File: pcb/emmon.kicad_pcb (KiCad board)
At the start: 2 copper layers, 47.3 x 67.2 mm, 48 parts, among them J1 PROG_CONN, J2 ANT_CONN, J3 AC_CONN, Q1 PT11-21C/L41/TR8, U1 DS3231SN, U2 CAT24C32WI-GT3, U3 LM393DR2G, U4 ESP-12E, U5 Ai-Thinker-Ra-01

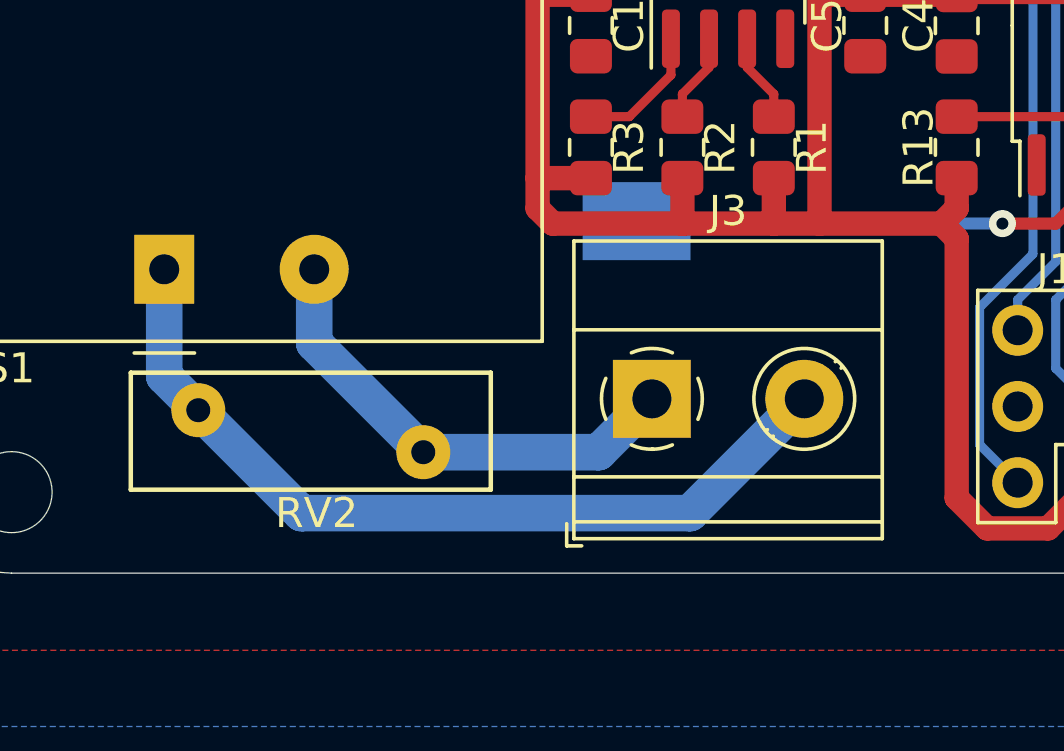
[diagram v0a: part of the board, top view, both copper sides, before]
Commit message: se corrige linea de AC
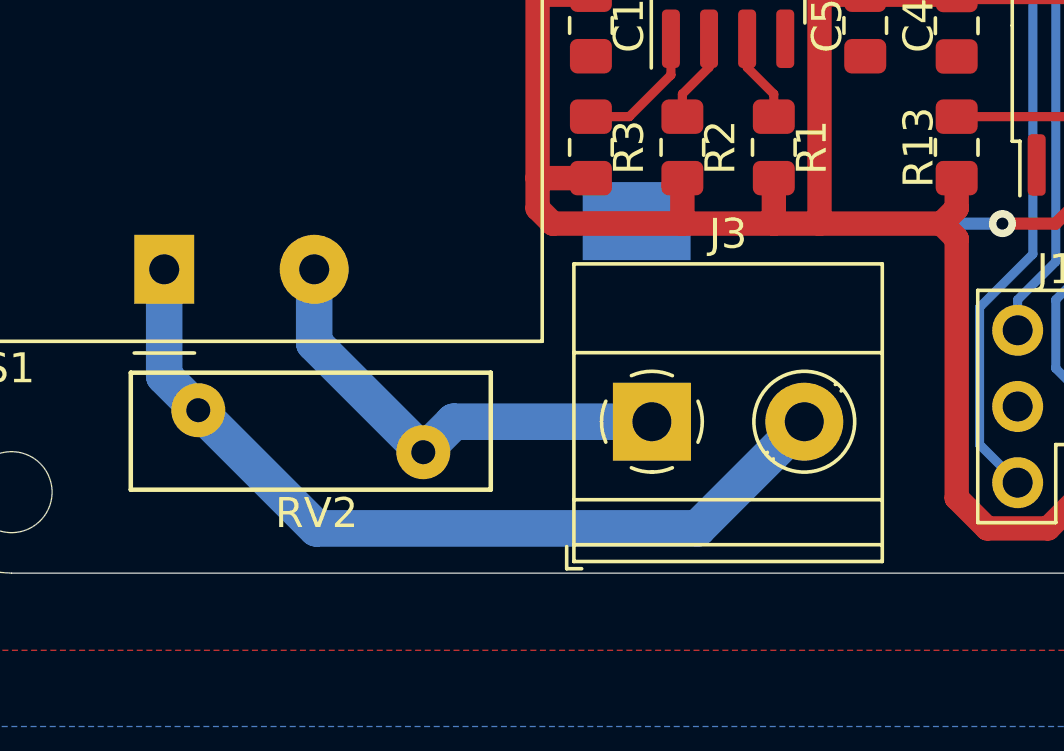
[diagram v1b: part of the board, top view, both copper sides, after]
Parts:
- moved J3 0.76 mm to (125.0, 125.5)

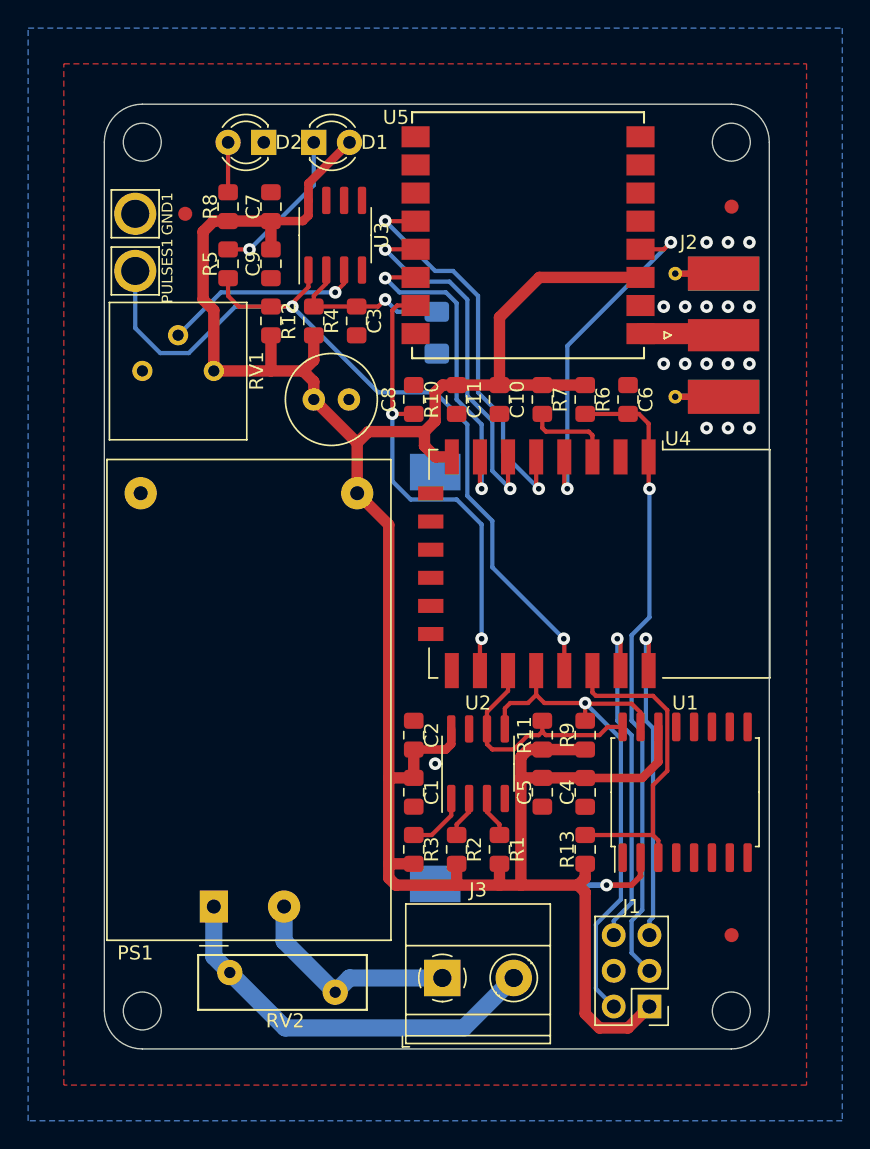
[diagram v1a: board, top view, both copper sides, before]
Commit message: se aplican las correciones de la revisión del profesor
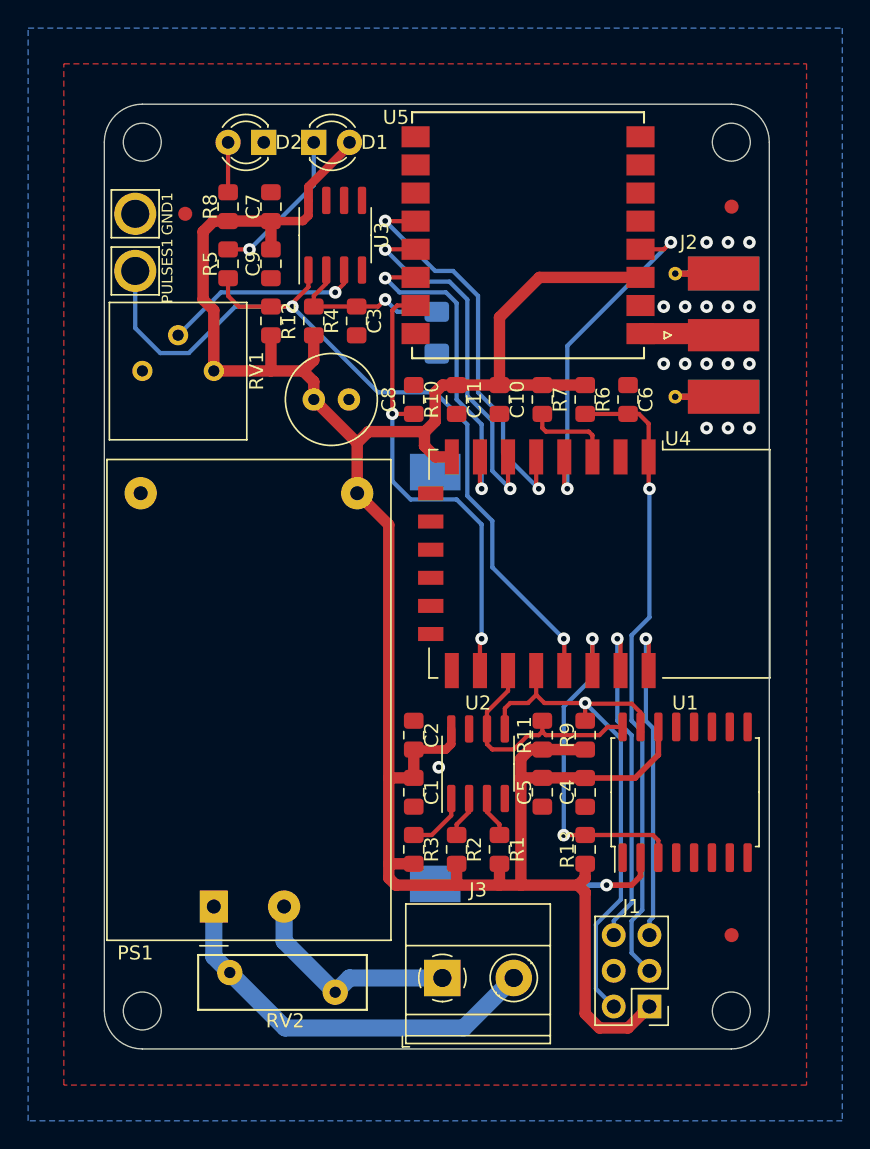
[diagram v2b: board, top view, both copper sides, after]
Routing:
- net /ALARM: track 23.3 -> 25.2 mm, vias 0 -> 2
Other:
- net class Default: clearance 0.1778 -> 0.254; trace_width 0.3048 -> 0.127; via_dia 0.9 -> 0.6; via_drill 0.4 -> 0.3
- rule trace_clearance: 0.1778 -> 0.254
- rule trace_min: 0.254 -> 0.127
- board text added: "Notas: - El borde del PCB se realizó según las medidas de la caja VG-S43 de la marca Vange. - La ubicación de los componentes se realizó priorizando que los conectores se encuentren en el borde de la placa y que U5 y J2 se encuentren lo más cerca posible entre ellos. - La ubicación de Q1 está bloqueada para que coincida con el agujero inferior de la caja."
- board text removed: "Notas: - El borde del PCB se realizó según las medidas de la caja VG-S43 de la marca Vange. - La ubicación de los componentes se realizó priorizando que los conector se encuentren en el borde de la placa y que U5 t J2 se ecuentren lo más cerca posible entre ellos. - La ubicación de Q1 está bloqueada para que coincida el agujero inferior de la caja"
